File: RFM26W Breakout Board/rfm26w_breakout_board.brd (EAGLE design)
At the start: 30.1 x 30.5 mm, 5 parts, among them X1 BU-SMA

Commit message: Layout updates.
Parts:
- moved X1 21.2 mm to (12.1, 26.0), turned to 0 degrees
- moved C1 14.5 mm to (5.71, 23.5), turned to 270 degrees
- moved JP2 10.0 mm to (22.2, 12.1)
- moved PCB 8.84 mm to (12.1, 10.8), turned to 0 degrees
- moved JP1 8.28 mm to (1.91, 10.8)
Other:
- board size 30.1 x 30.5 mm -> 24.1 x 30.5 mm
- board text added: "BREAKOUT"

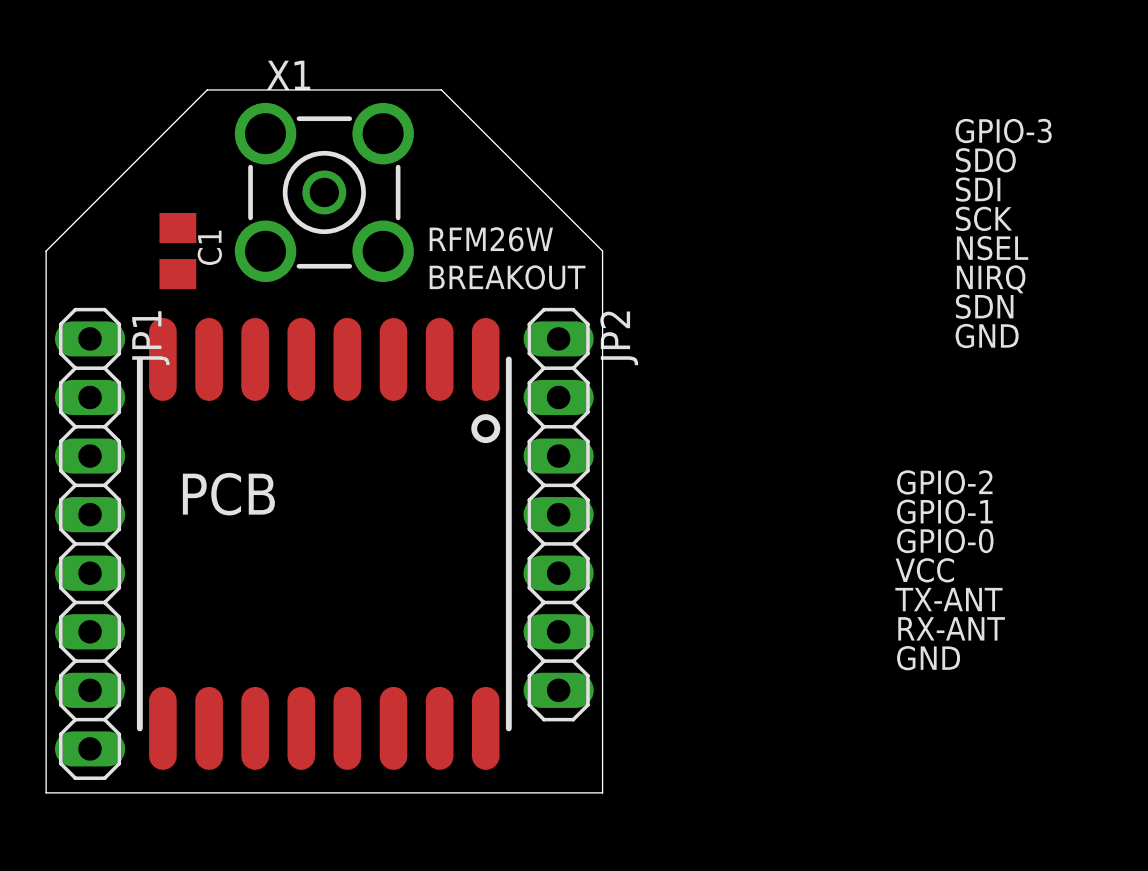
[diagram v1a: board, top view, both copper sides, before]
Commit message: Routed the RFM26W Breakout Board.
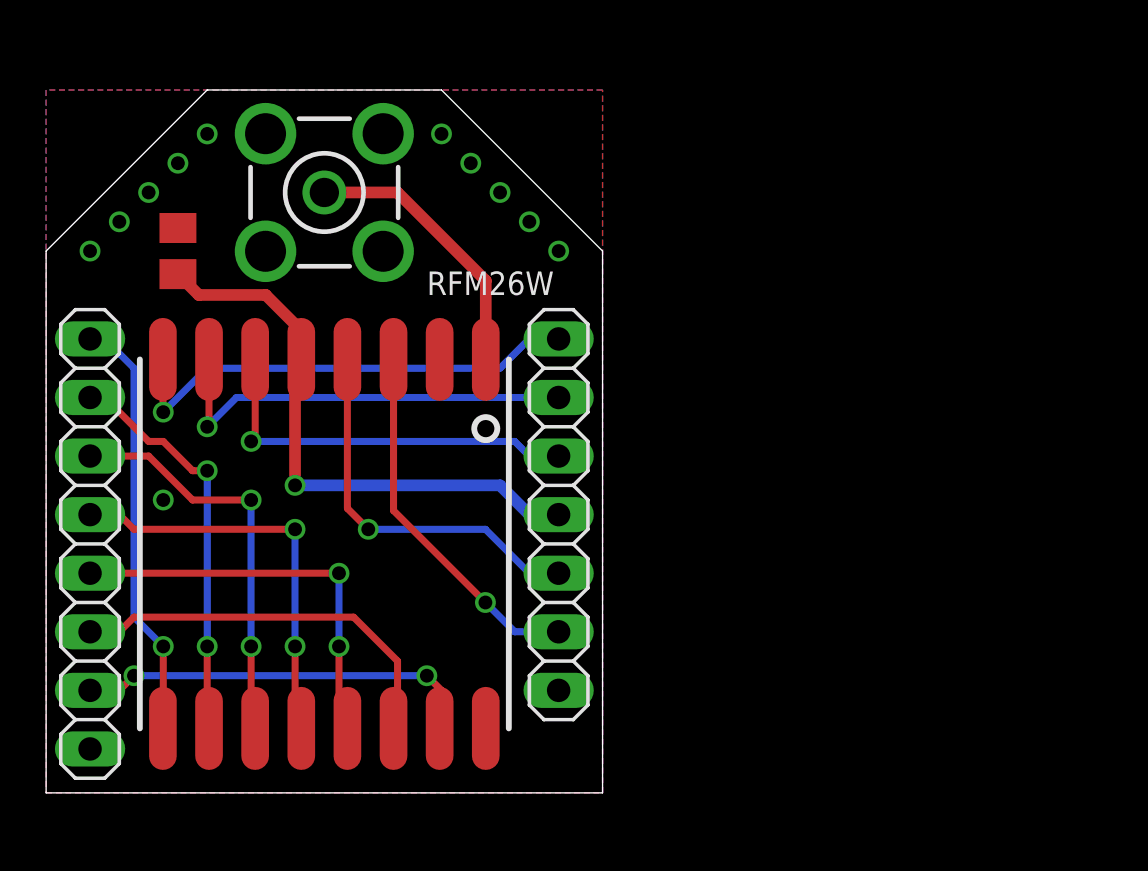
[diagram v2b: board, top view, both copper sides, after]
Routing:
- net VCC: track 0.00 -> 25.3 mm, vias 0 -> 1
- net GPIO-2: track 0.00 -> 20.7 mm, vias 0 -> 1
- net GPIO-1: track 0.00 -> 18.7 mm, vias 0 -> 1
- net GPIO-3: track 0.00 -> 18.6 mm, vias 0 -> 1
- net SCK: track 0.00 -> 17.9 mm, vias 0 -> 2
- net SDI: track 0.00 -> 17.8 mm, vias 0 -> 2
- net NSEL: track 0.00 -> 17.7 mm, vias 0 -> 2
- net SDO: track 0.00 -> 17.6 mm, vias 0 -> 2
- net SDN: track 0.00 -> 17.4 mm, vias 0 -> 2
- net NIRQ: track 0.00 -> 17.4 mm
- net GPIO-0: track 0.00 -> 17.2 mm, vias 0 -> 1
- net TX-ANT: track 0.00 -> 16.8 mm, vias 0 -> 1
- net RX-ANT: track 0.00 -> 15.9 mm, vias 0 -> 1
- net ANT: track 0.00 -> 12.0 mm
- added copper zone on layer 1, net GND
- added copper zone on layer 16, net GND
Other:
- board text added: "CC-BY-SA 4.0 KAI C. BADER"
- board text removed: "BREAKOUT"
